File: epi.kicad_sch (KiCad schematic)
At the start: 28 parts, among them J1 Connector 1x12, J2 Connector 1x12, J3 Connector 1x04, J4 USB-C 2.0 mid-mount female co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, U1 ATmega32U4-M, Y1 16mhz

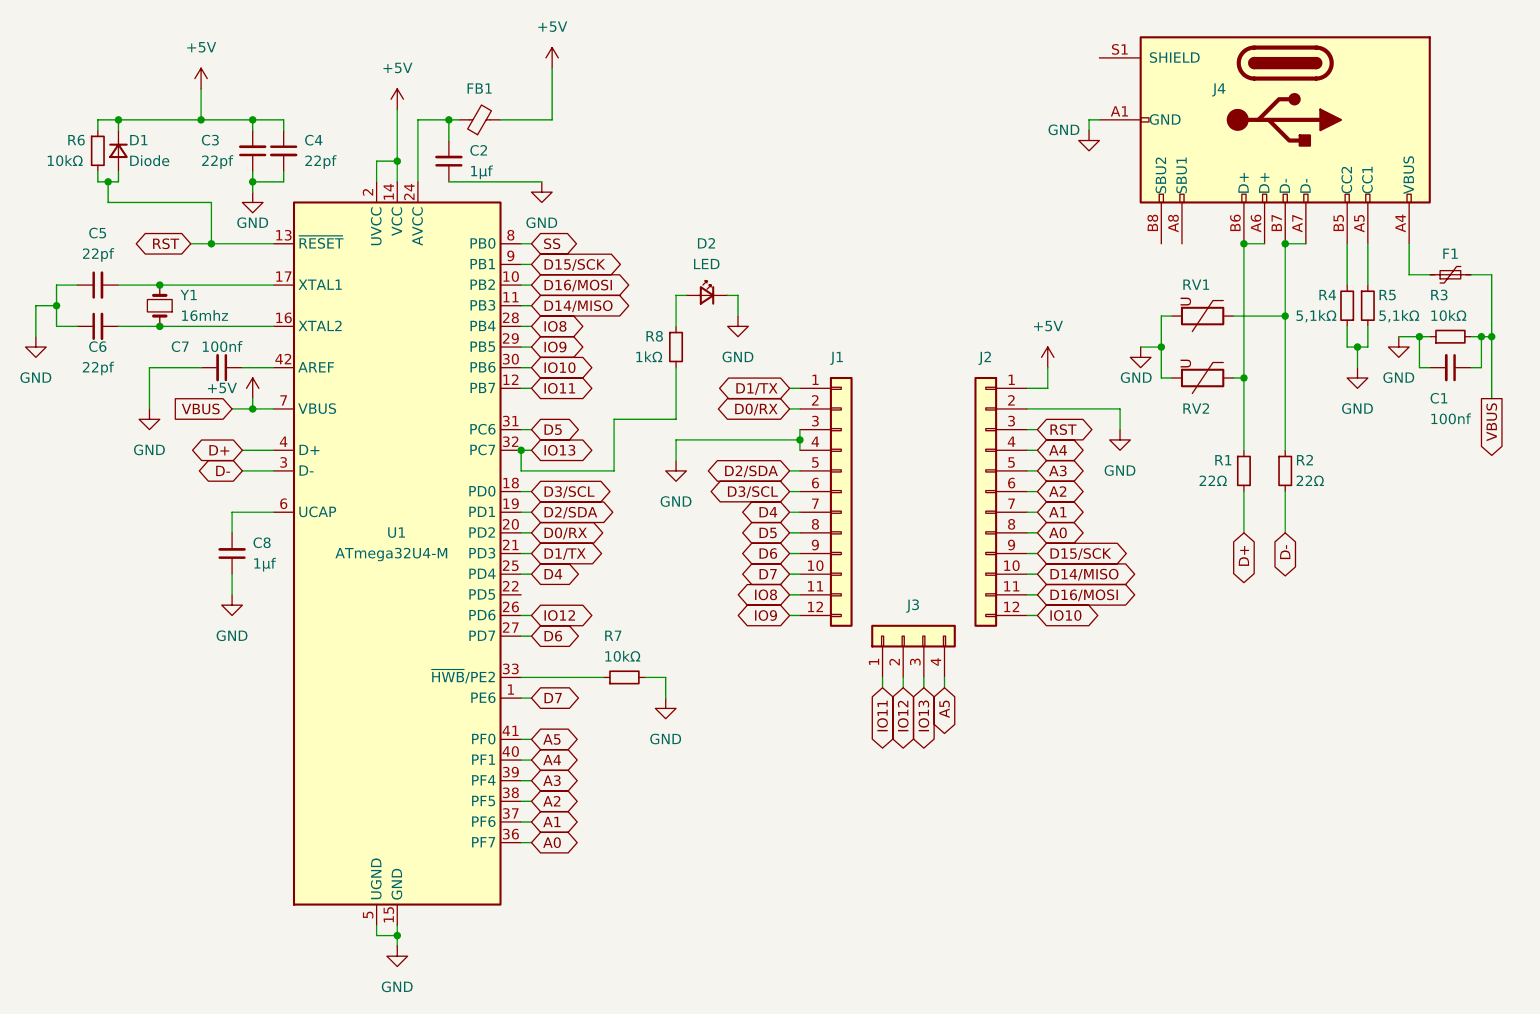
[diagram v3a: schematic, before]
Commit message: increased trace spacing and a few other changes
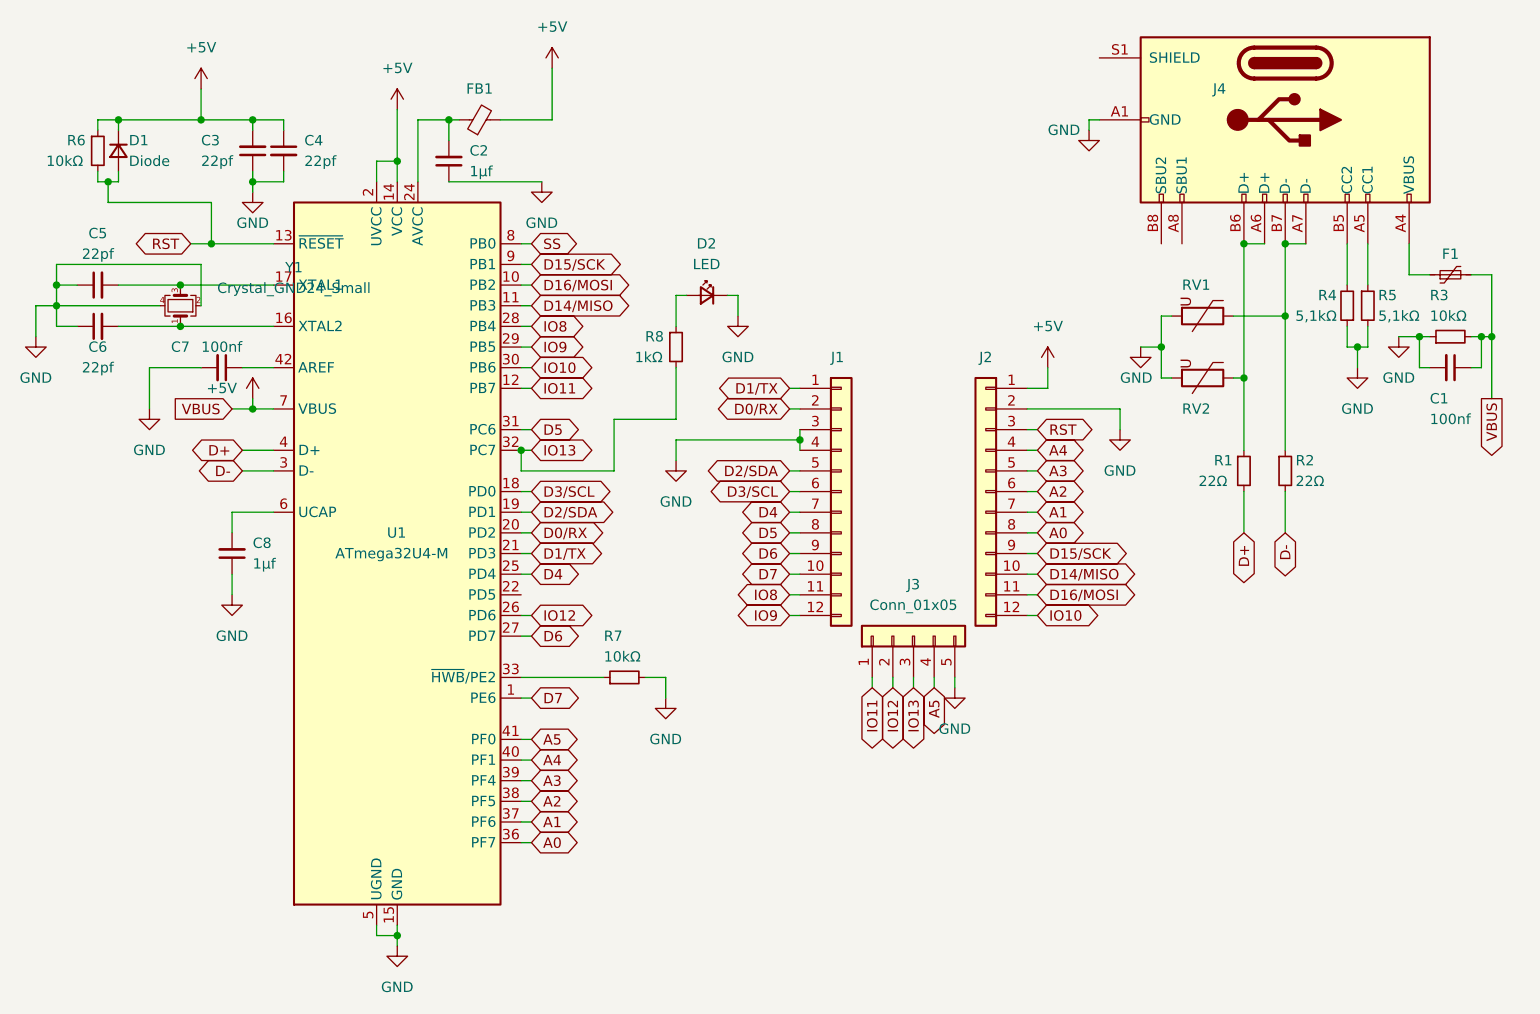
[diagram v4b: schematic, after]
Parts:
- removed J3: Connector 1x04, Connector_PinHeader_1.27mm:PinHeader_1x04_P1.27mm_Vertical, symbol Connector_Generic:Conn_01x04
- removed Y1: 16mhz, Crystal:Crystal_SMD_2016-4Pin_2.0x1.6mm, symbol Device:Crystal_Small
- added J3: Conn_01x05, Connector_PinHeader_1.27mm:PinHeader_1x05_P1.27mm_Vertical, symbol Connector_Generic:Conn_01x05
- added Y1: Crystal_GND24_Small, Crystal:Crystal_SMD_2016-4Pin_2.0x1.6mm, symbol Device:Crystal_GND24_Small
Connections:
- net A5: now also J3.4 (Pin_4)
- net GND: now also J3.5 (Pin_5), Y1.2, Y1.4
- net IO11: now also J3.1 (Pin_1)
- net IO12: now also J3.2 (Pin_2)
- net IO13: now also J3.3 (Pin_3)
- net at C6.2, U1.16 (XTAL2): now also Y1.1
- net at C5.2, U1.17 (XTAL1): now also Y1.3
